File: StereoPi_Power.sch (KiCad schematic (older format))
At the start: 92 parts, among them SW1 SW_SPDT

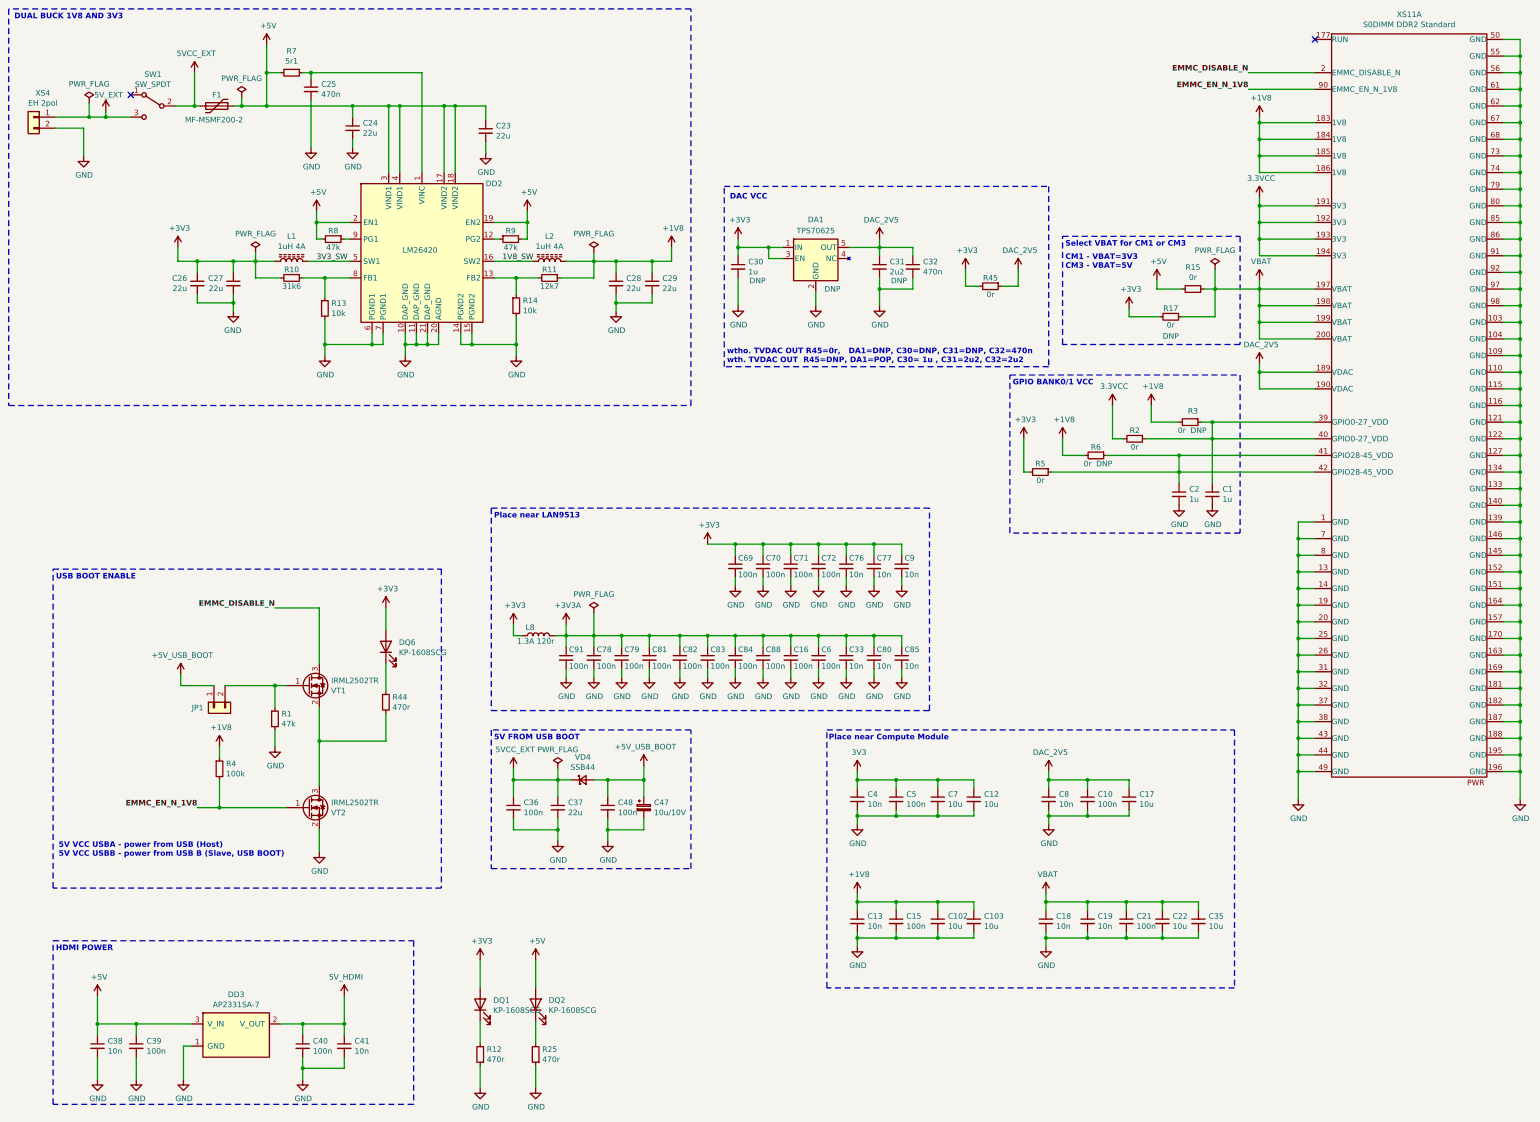
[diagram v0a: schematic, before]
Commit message: added Voltages to Caps, reformatted labels
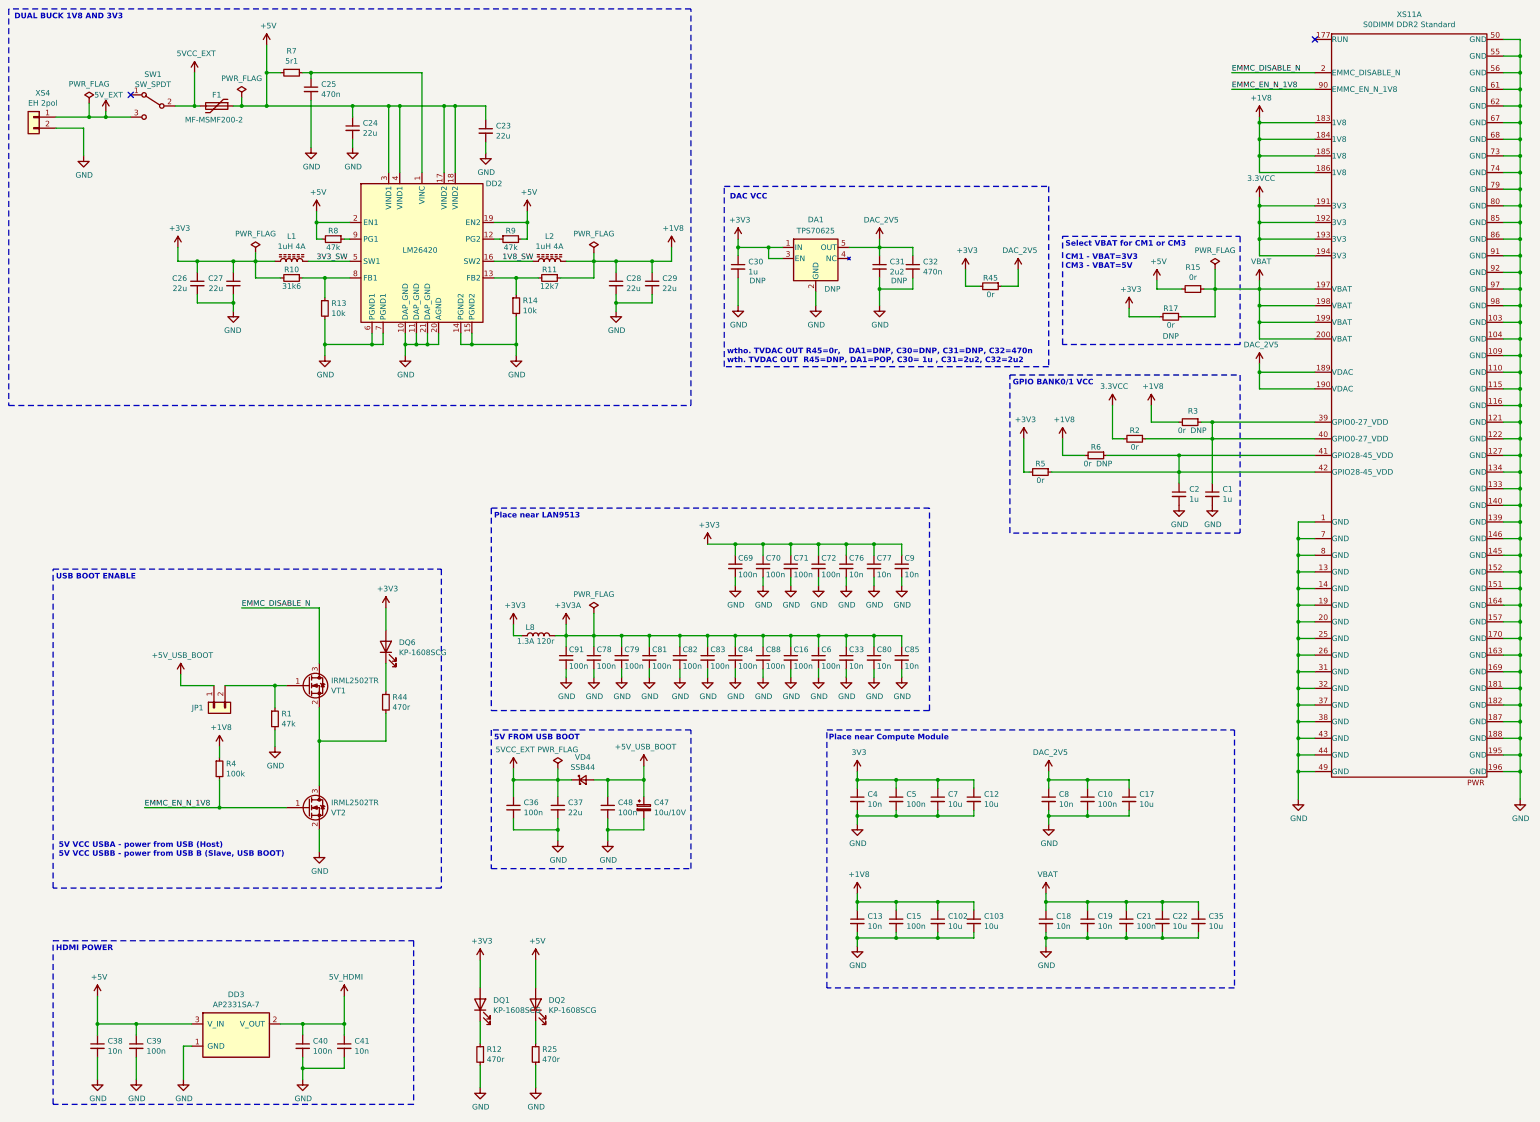
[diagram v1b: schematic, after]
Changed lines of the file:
@@
 EESchema Schematic File Version 4
 LIBS:StereoPi-cache
-EELAYER 26 0
+EELAYER 30 0
 EELAYER END
 $Descr A3 16535 11693
@@
 	14475 1025 14325 1025
 Wire Wire Line
-	12625 1325 12025 1325
-Wire Wire Line
-	12625 1475 12025 1475
+	12625 1325 11875 1325
+Wire Wire Line
+	12625 1475 11875 1475
 $Comp
 L Connector_Generic:Conn_01x02 JP?
@@
 	2800 6850 3250 6850
 Wire Wire Line
-	3250 6150 3650 6150
+	2950 6150 3650 6150
 Wire Wire Line
 	3650 6150 3650 6650
@@
 	2750 7500 2750 7400
 Wire Wire Line
-	2550 7950 2750 7950
+	2075 7950 2750 7950
 Connection ~ 2750 7950
 $Comp
@@
 Text Notes 1300 8400 0    50   ~ 10
 5V VCC USBA - power from USB (Host)\n5V VCC USBB - power from USB B (Slave, USB BOOT)
-Text Label 12025 1325 2    50   ~ 10
+Text Label 11875 1325 0    50   ~ 0
 EMMC_DISABLE_N
-Text Label 12025 1475 2    50   ~ 10
+Text Label 11875 1475 0    50   ~ 0
 EMMC_EN_N_1V8
-Text Label 3250 6150 2    50   ~ 10
+Text Label 2950 6150 0    50   ~ 0
 EMMC_DISABLE_N
-Text Label 2550 7950 2    50   ~ 10
+Text Label 2075 7950 0    50   ~ 0
 EMMC_EN_N_1V8
 $Comp
